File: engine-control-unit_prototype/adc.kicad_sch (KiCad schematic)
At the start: 30 parts, among them J4 PT1, J5 VREF, J6 PT1, J7 VREF, U3 INA826, U4 INA826

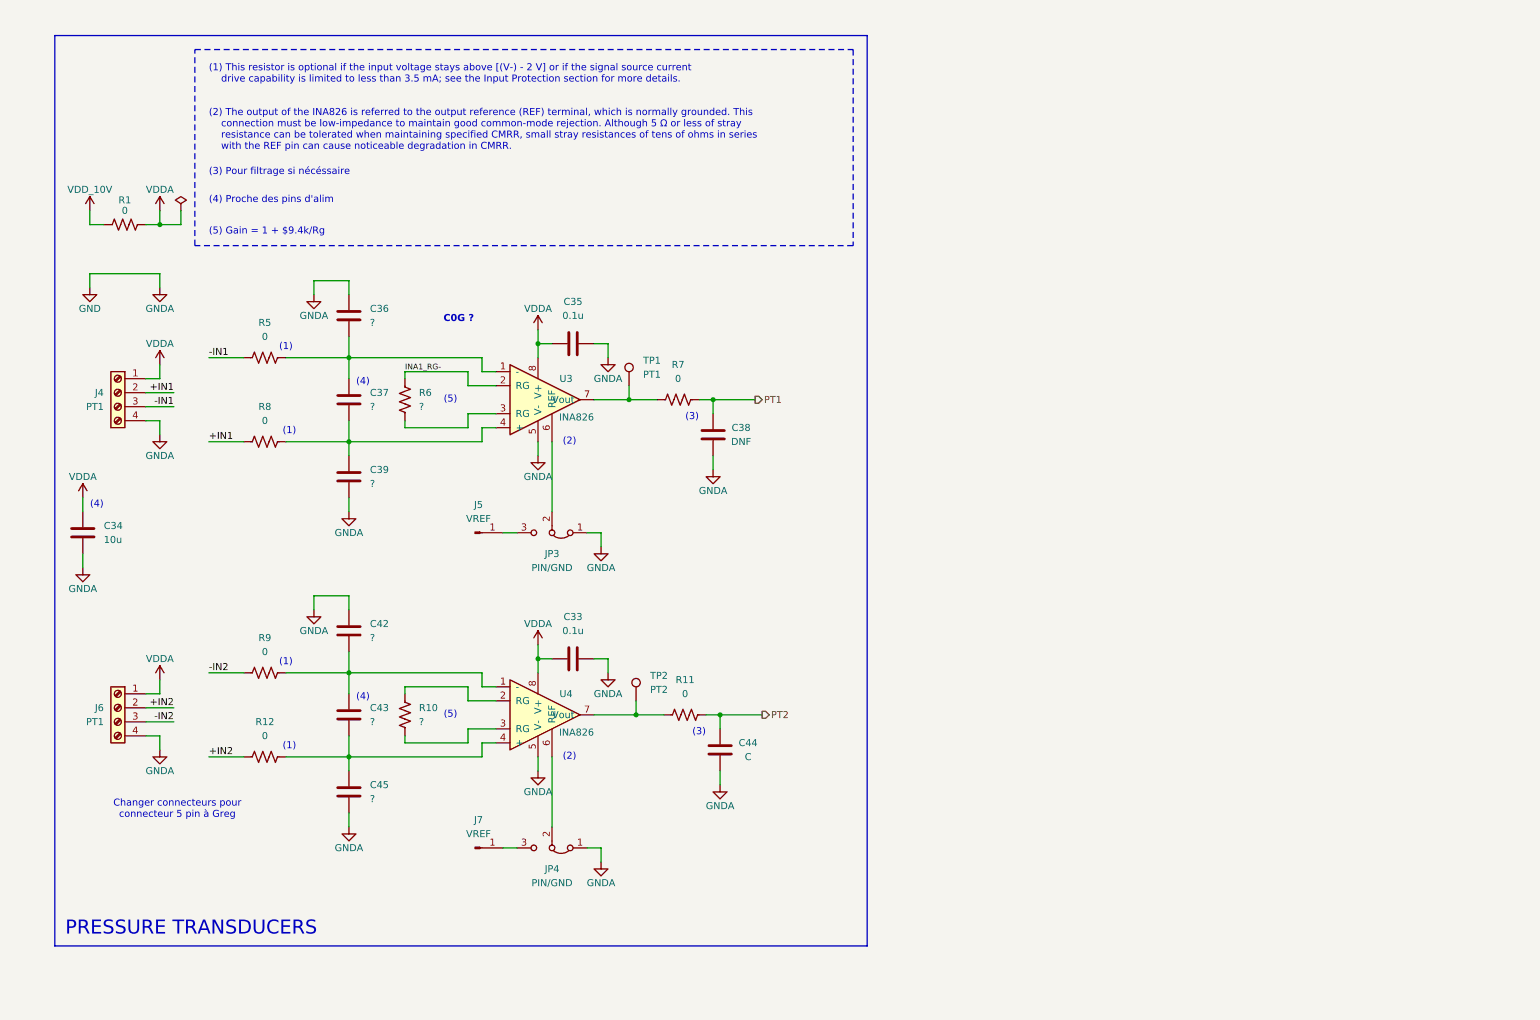
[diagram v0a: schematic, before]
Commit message: Added subsheets
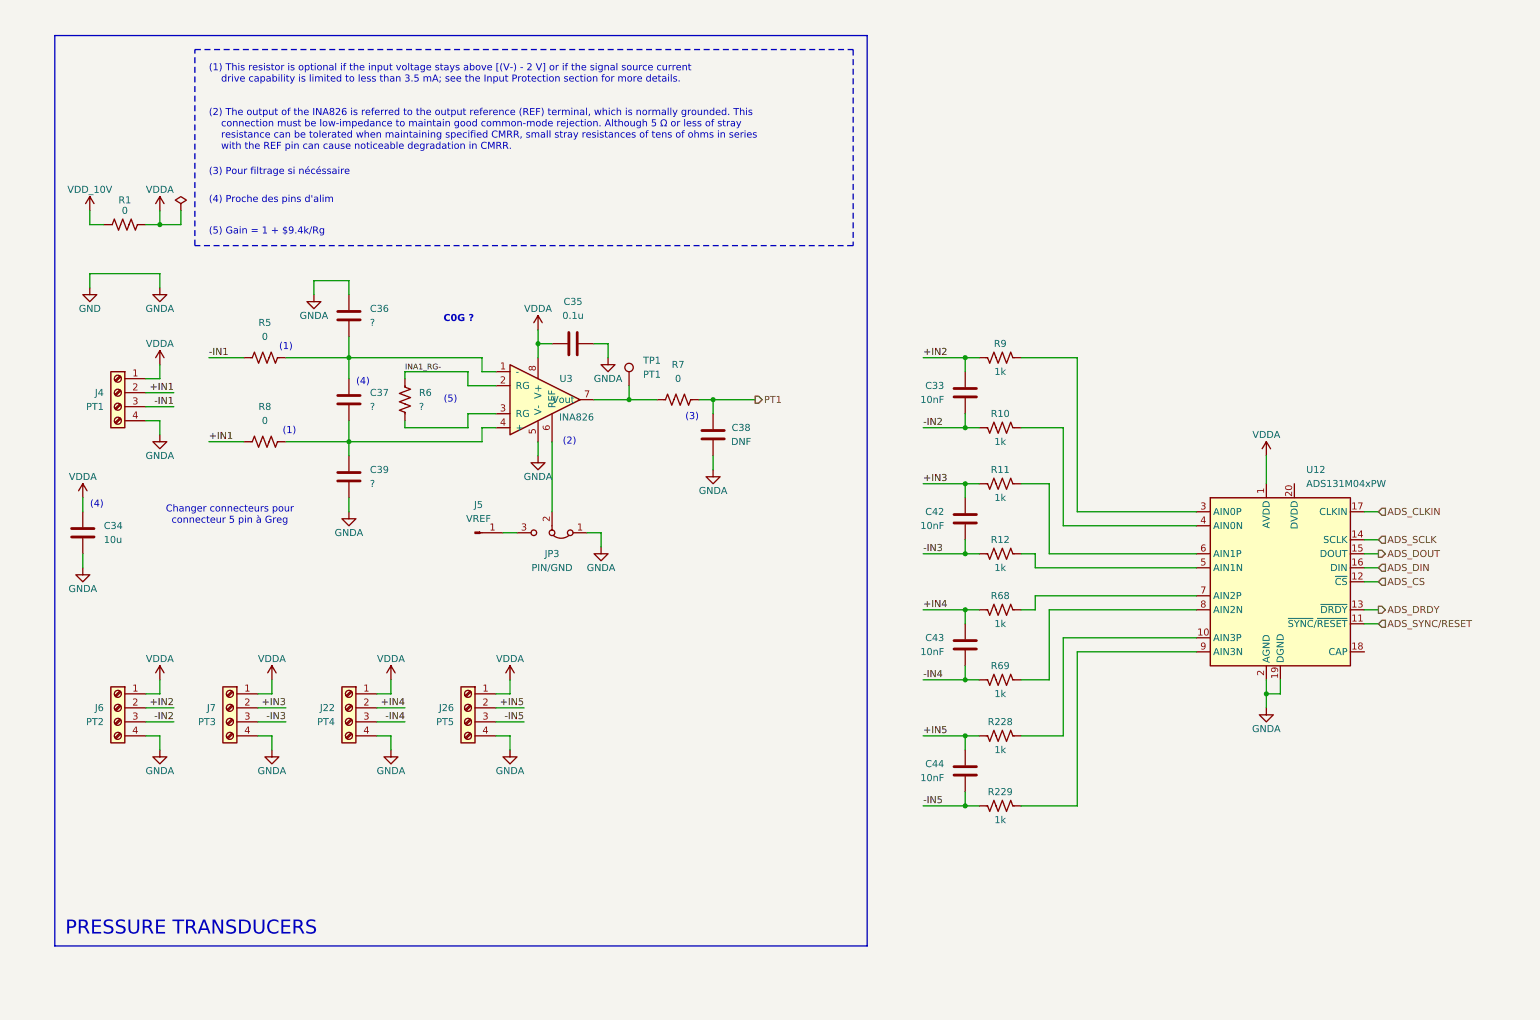
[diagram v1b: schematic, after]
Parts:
- removed C45: ?, symbol Device:C
- removed J7: VREF, symbol Connector:Conn_01x01_Pin
- removed JP4: PIN/GND, symbol Jumper:Jumper_3_Bridged12
- removed TP2: PT2, symbol Connector:TestPoint
- removed U4: INA826, UserFootprints:SOP65P490X110-8N, symbol INA826:INA826AIDGKR
- added J22: PT4, symbol Connector:Screw_Terminal_01x04
- added J26: PT5, symbol Connector:Screw_Terminal_01x04
- added J7: PT3, symbol Connector:Screw_Terminal_01x04
- added R228, R229, R68, R69: 1k, symbol Device:R_US
- added U12: ADS131M04xPW, Package_SO:TSSOP-20_4.4x6.5mm_P0.65mm, symbol Analog_ADC:ADS131M04xPW
- C33: value 0.1u -> 10nF
- C42, C43: value ? -> 10nF
- C44: value C -> 10nF
- J6: value PT1 -> PT2
- R10: value ? -> 1k
- R11, R12, R9: value 0 -> 1k
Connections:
- net +IN2: now also C33.2, R9.2; no longer R12.2
- net -IN2: now also C33.1, R10.2; no longer R9.2
- net GND: now also J22.4 (Pin_4), J26.4 (Pin_4), J7.4 (Pin_4), U12.19 (DGND), U12.2 (AGND); no longer C33.1, C42.2, C44.1
- net VDDA: now also J22.1 (Pin_1), J26.1 (Pin_1), J7.1 (Pin_1), U12.1 (AVDD); no longer C33.2
- net +IN3: now reaches R11.2
- net +IN3: now also C42.2, J7.2 (Pin_2)
- net at R12.1: now also U12.5 (AIN1N); no longer C43.1
- net at R10.1: now also U12.4 (AIN0N)
- net PT2: no longer names the net of R11.1
- net PT2: now also U12.6 (AIN1P); no longer C44.2
- new net: R228.1, U12.10 (AIN3P)
- new net: R69.1, U12.8 (AIN2N)
- new net: R9.1, U12.3 (AIN0P)
- new net: R68.1, U12.7 (AIN2P)
- new net: R229.1, U12.9 (AIN3N)
- new net +IN4: C43.2, J22.2 (Pin_2), R68.2
- new net +IN5: C44.2, J26.2 (Pin_2), R228.2
- new net -IN3: C42.1, J7.3 (Pin_3), R12.2
- new net -IN4: C43.1, J22.3 (Pin_3), R69.2
- new net -IN5: C44.1, J26.3 (Pin_3), R229.2
- new net ADS_CLKIN: U12.17 (CLKIN)
- new net ADS_CS: U12.12 (~{CS})
- new net ADS_DIN: U12.16 (DIN)
- new net ADS_DOUT: U12.15 (DOUT)
- new net ADS_DRDY: U12.13 (~{DRDY})
- new net ADS_SCLK: U12.14 (SCLK)
- new net ADS_SYNC/RESET: U12.11 (~{SYNC}/~{RESET})

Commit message: Added Control page Revisited power tree (VDDA_3V3 and VDD_3V3) Bunch of other fixes
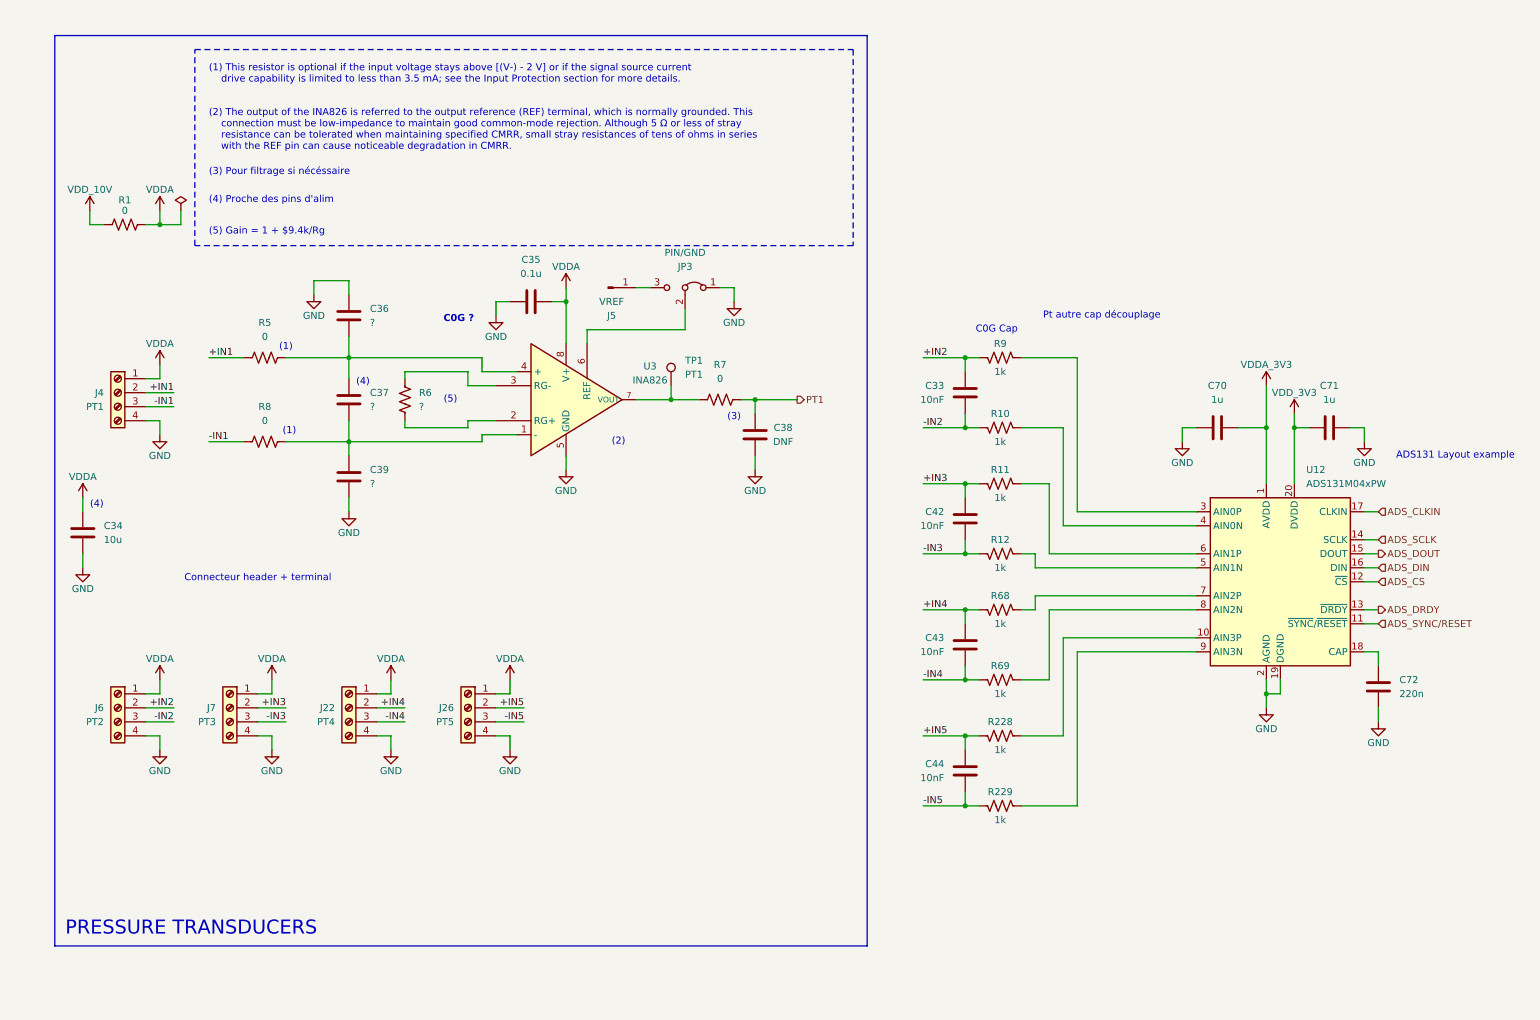
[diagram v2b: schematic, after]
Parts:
- removed U3: INA826, UserFootprints:SOP65P490X110-8N, symbol INA826:INA826AIDGKR
- added C70, C71: 1u, Capacitor_SMD:C_0603_1608Metric, symbol Device:C
- added C72: 220n, Capacitor_SMD:C_0603_1608Metric, symbol Device:C
- added U3: INA826, Package_SO:SOIC-8-1EP_3.9x4.9mm_P1.27mm_EP2.29x3mm, symbol SiriusLib:INA826
- C33: footprint (none) -> Capacitor_SMD:C_0402_1005Metric
- C34, C35, C36, C37, C38, C39, C42, C43, C44: footprint (none) -> Capacitor_SMD:C_0603_1608Metric
- R1, R5, R7, R8: footprint (none) -> Resistor_SMD:R_0201_0603Metric
- R10, R11, R12, R6, R68, R69, R9: footprint (none) -> Resistor_SMD:R_0603_1608Metric
- R228, R229: footprint (none) -> Resistor_SMD:R_0402_1005Metric
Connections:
- net +IN1: now also R5.2; no longer R8.2
- net -IN1: now also R8.2; no longer R5.2
- net GND: now also C70.1, C71.2, C72.1, U3.5 (GND)
- net VDDA: now also U3.8 (V+); no longer U12.1 (AVDD)
- net at C37.1, C39.2, R8.1: now also U3.1 (-)
- net at C36.1, C37.2, R5.1: now also U3.4 (+)
- net at R7.2, TP1.1: now also U3.7 (VOUT)
- net at U12.18 (CAP): now also C72.2
- net VDD_3V3: now reaches U12.20 (DVDD)
- net VDD_3V3: now also C71.1
- net at JP3.2 (C): now also U3.6 (REF)
- net at R6.1: now also U3.2 (RG+)
- net INA1_RG-: no longer names the net of R6.2
- net INA1_RG-: now also U3.3 (RG-)
- new net VDDA_3V3: C70.2, U12.1 (AVDD)
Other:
- note added: "ADS131 Layout example"
- note added: "C0G Cap"
- note added: "Connecteur header + terminal"
- note added: "Pt autre cap découplage"
- note removed: "Changer connecteurs pour connecteur 5 pin à Greg"
- moved on the sheet: C35, C38, J5, JP3, R7, TP1

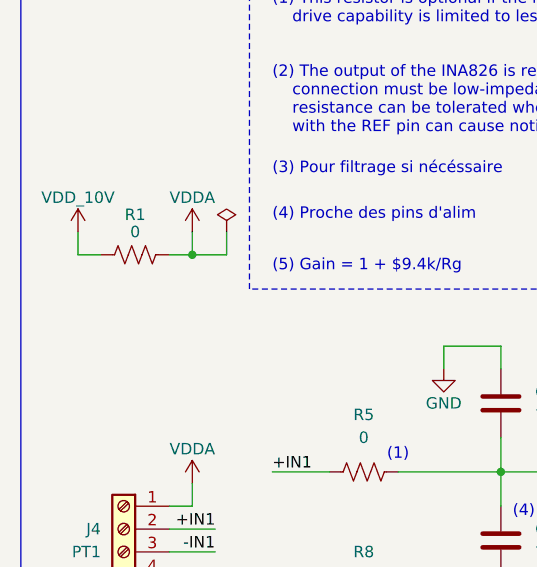
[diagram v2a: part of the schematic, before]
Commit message: Fixed inverted LED diodes (oops) Replaced 3x INA219 with INA3221
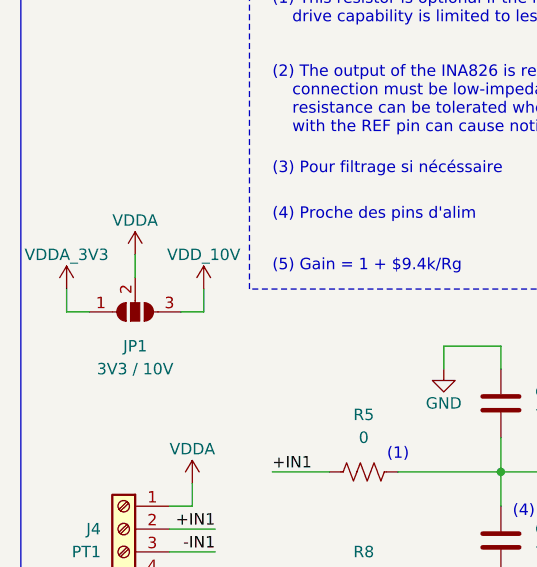
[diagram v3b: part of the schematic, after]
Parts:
- removed R1: 0, Resistor_SMD:R_0201_0603Metric, symbol Device:R_US
- added JP1: 3V3 / 10V, symbol Jumper:SolderJumper_3_Open
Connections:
- net VDDA: now also JP1.2 (C)
- net VDDA_3V3: now also JP1.1 (A)
- net VDD_10V: now also JP1.3 (B)

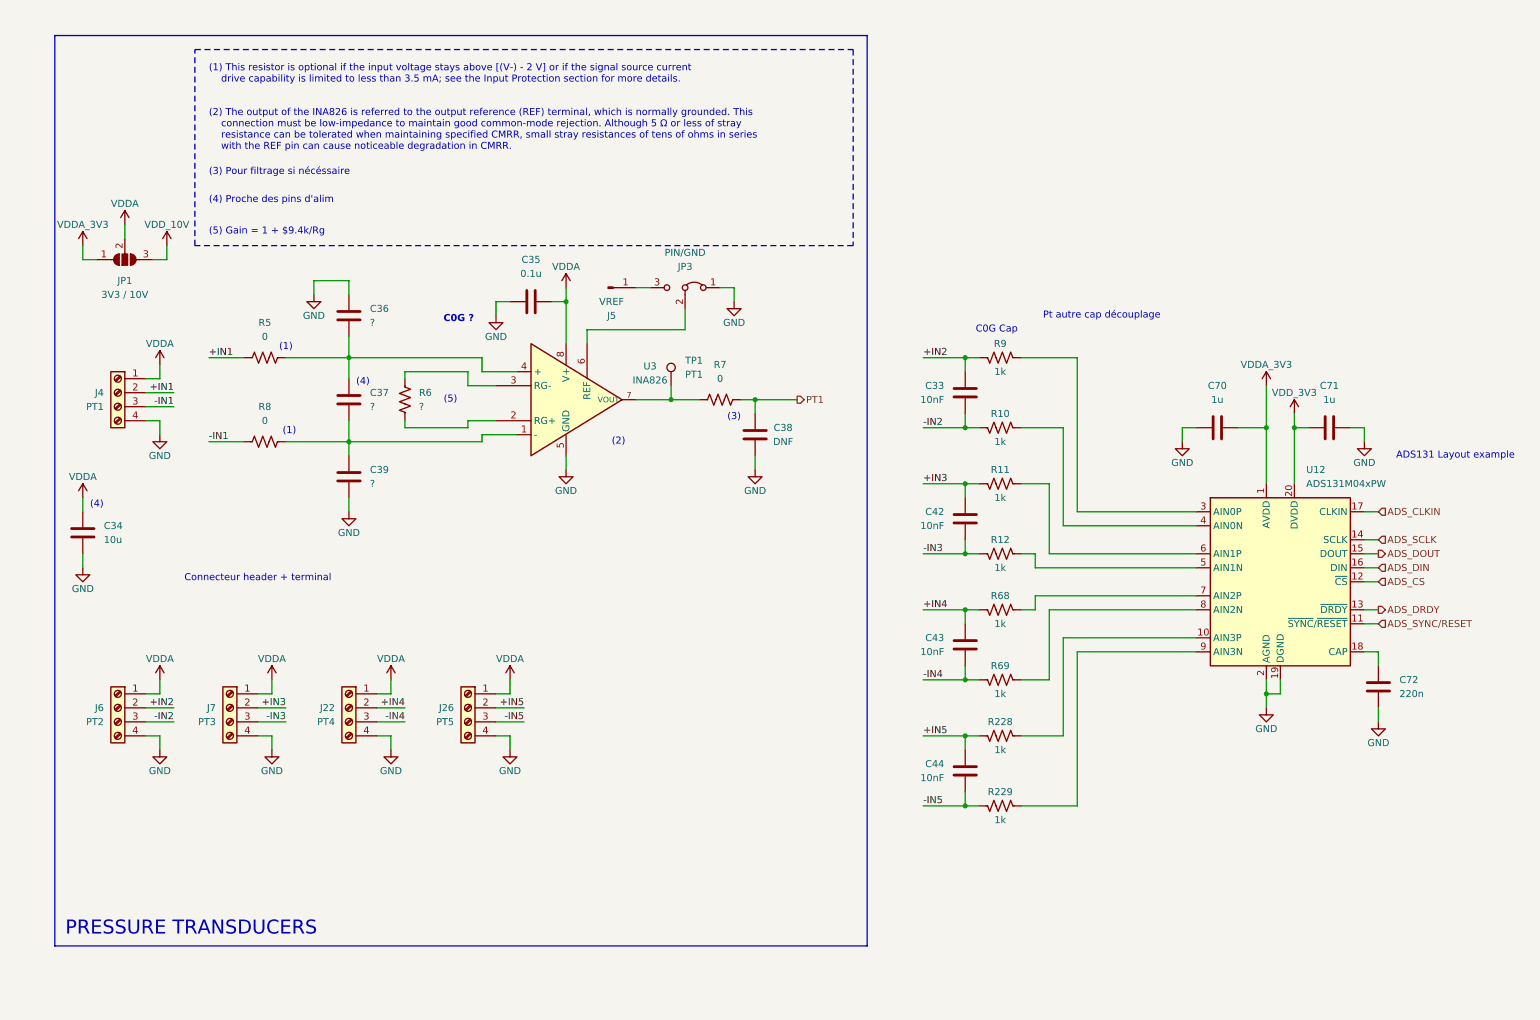
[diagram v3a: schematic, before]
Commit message: Added magnetic encoders Added optional external valve control connector
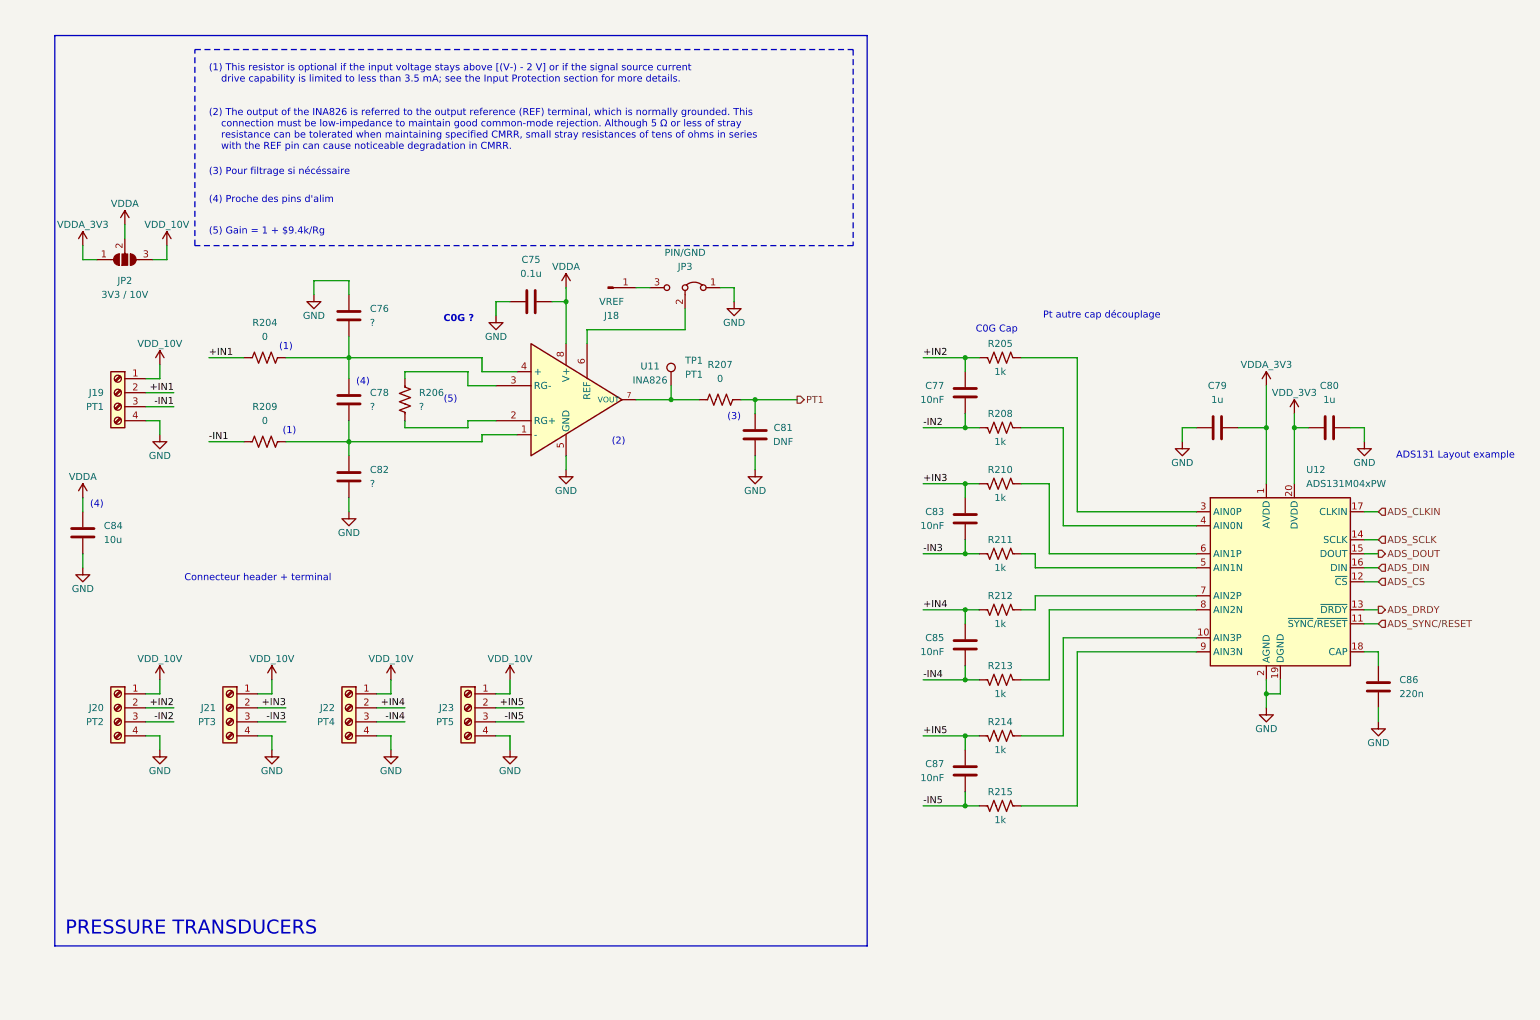
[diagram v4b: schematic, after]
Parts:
- renumbered C35 to C75, C36 to C76, C33 to C77, C37 to C78, C70 to C79, C71 to C80, C38 to C81, C39 to C82, C42 to C83, C34 to C84, C43 to C85, C72 to C86, C44 to C87, J5 to J18, J4 to J19, J6 to J20, J7 to J21, J26 to J23, JP1 to JP2, R5 to R204, R9 to R205, R6 to R206, R7 to R207, R10 to R208, R8 to R209, R11 to R210, R12 to R211, R68 to R212, R69 to R213, R228 to R214, R229 to R215, U3 to U11
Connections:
- net VDDA: no longer J19.1 (Pin_1), J20.1 (Pin_1), J21.1 (Pin_1), J22.1 (Pin_1), J23.1 (Pin_1)
- net VDD_10V: now also J19.1 (Pin_1), J20.1 (Pin_1), J21.1 (Pin_1), J22.1 (Pin_1), J23.1 (Pin_1)
